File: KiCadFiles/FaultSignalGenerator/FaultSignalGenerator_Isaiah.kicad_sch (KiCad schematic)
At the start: 12 parts, among them U1 OPAMP, U2 TL074CDR

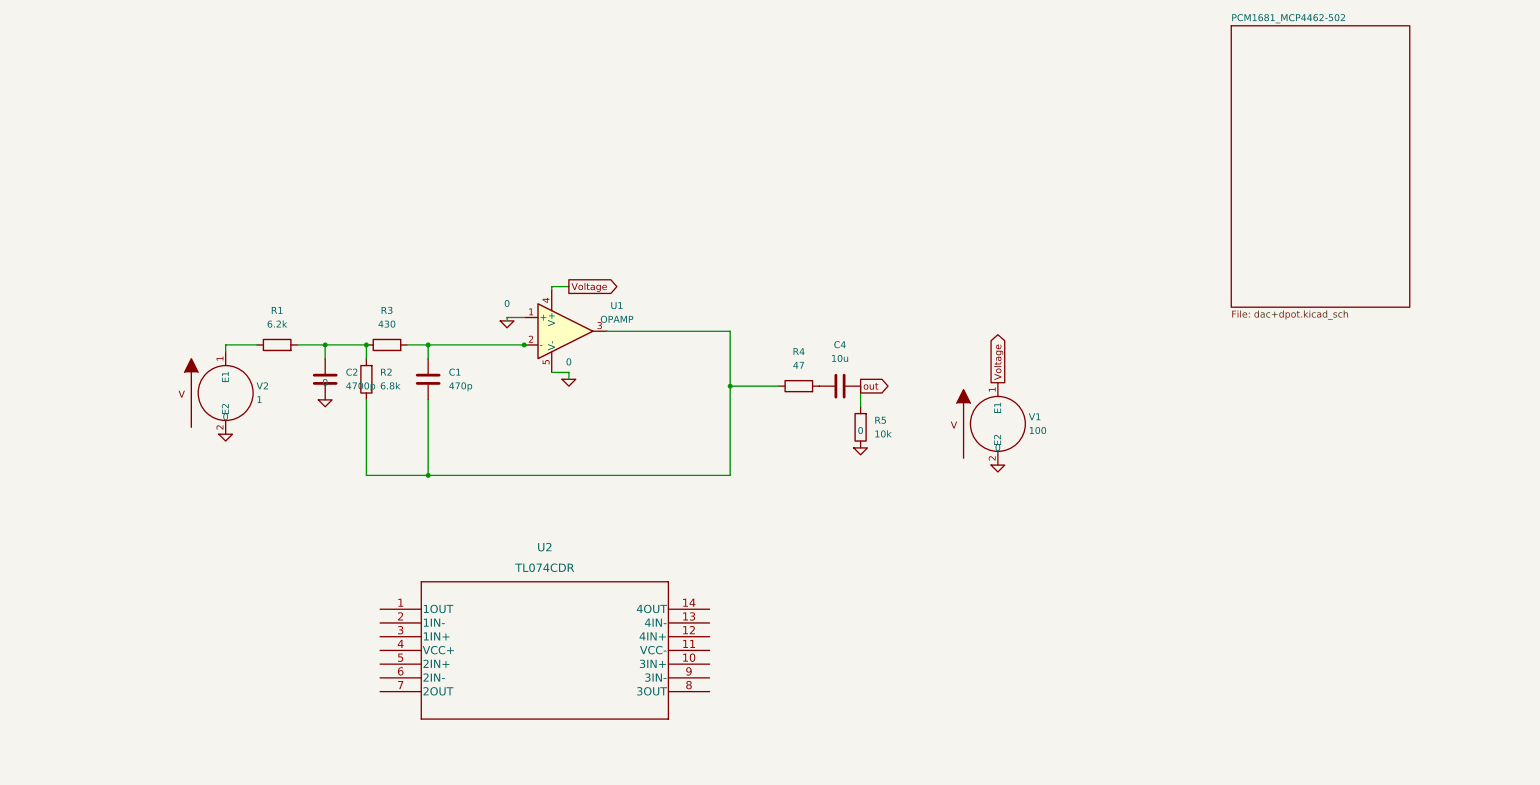
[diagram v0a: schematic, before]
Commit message: Schema push
Got my account stuff sorted out. Push should work now. Still am trying to figure out why my components aren't auto-generating footprints for use in the PCB editor.
Apologies for the messiness.
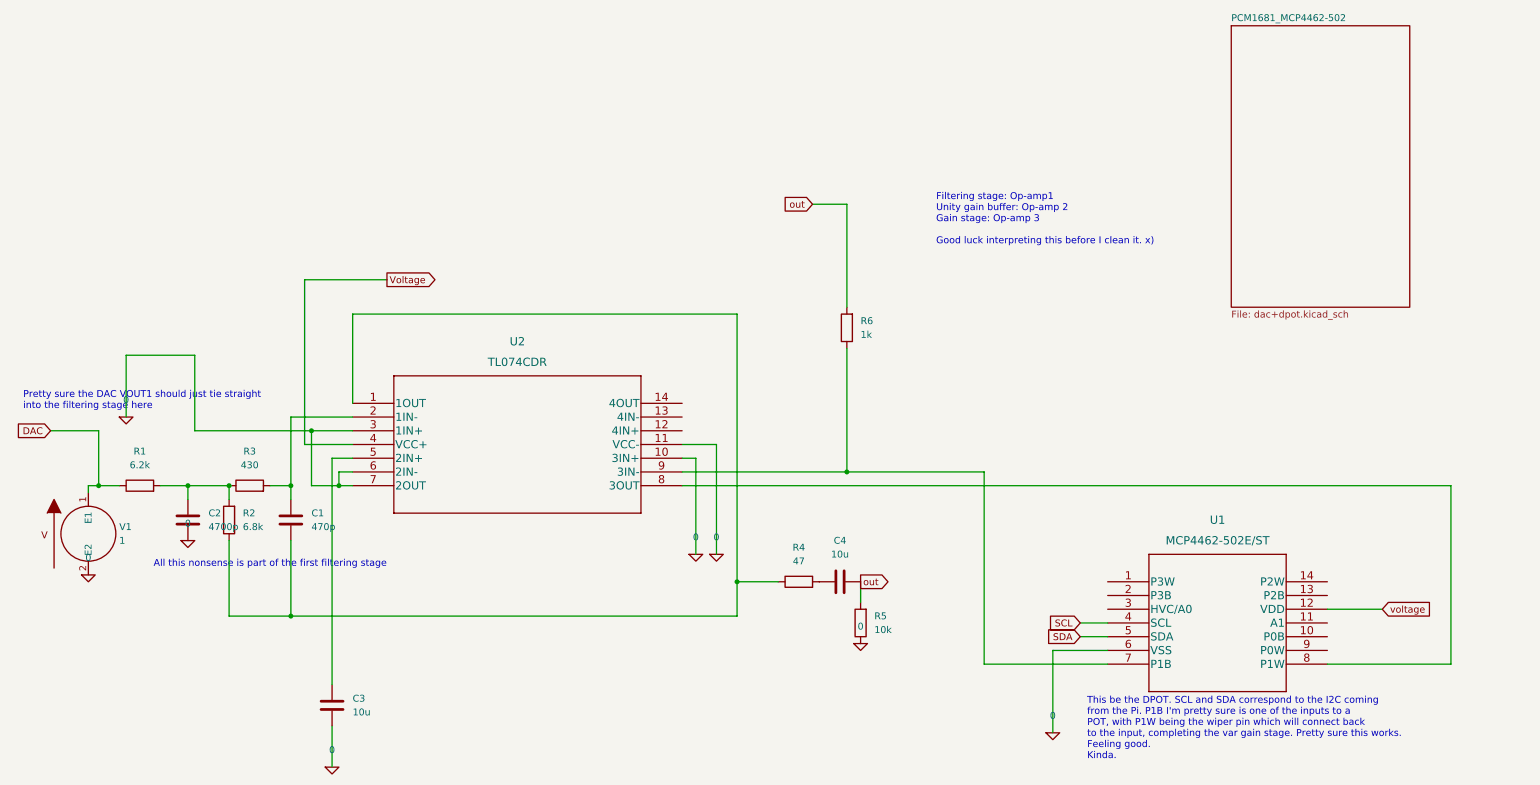
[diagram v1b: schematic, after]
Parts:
- removed U1: OPAMP, symbol Simulation_SPICE:OPAMP
- removed V2: 1, symbol pspice:VSOURCE
- added C3: 10u, symbol Device:C
- added R6: 1k, symbol Device:R
- added U1: MCP4462-502E/ST, TSSOP14_MC_MCH, symbol 2023-01-31_02-59-41:MCP4462-502E/ST
- V1: value 100 -> 1; Spice_Model dc 12 -> dc 50 ac 3
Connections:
- net 0: now also U2.10 (3IN+), U2.11 (VCC-), U2.3 (1IN+), U2.6 (2IN-), U2.7 (2OUT), C3.1, U1.6 (VSS)
- net Voltage: now also U2.4 (VCC+); no longer V1.1 (E1)
- net out: now also R6.2
- net DAC: now reaches R1.1
- net DAC: now also V1.1 (E1)
- net at C1.1, R3.2: now also U2.2 (1IN-)
- net at C1.2, R2.1, R4.1: now also U2.1 (1OUT)
- net at U2.5 (2IN+): now also C3.2
- net at U2.8 (3OUT): now also U1.8 (P1W)
- net at U2.9 (3IN-): now also R6.1, U1.7 (P1B)
- new net SCL: U1.4 (SCL)
- new net SDA: U1.5 (SDA)
- new net voltage: U1.12 (VDD)
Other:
- note added: "All this nonsense is part of the first filtering stage"
- note added: "Filtering stage: Op-amp1 Unity gain buffer: Op-amp 2 Gain stage: Op-amp 3 Good luck interpreting this before I clean it. x)"
- note added: "Pretty sure the DAC VOUT1 should just tie straight into the filtering stage here"
- note added: "This be the DPOT. SCL and SDA correspond to the I2C coming from the Pi. P1B I'm pretty sure is one of the inputs to a POT, with P1W being the wiper pin which will connect back to the input, completing the var gain stage. Pretty sure this works. Feeling good. Kinda."
- moved on the sheet: U2

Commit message: test push
Fully foot-printed schematic
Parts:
- removed V1: 1, symbol pspice:VSOURCE
- C1: renamed from C2; value 4700p -> 4700pF; footprint (none) -> Capacitor_SMD:C_1812_4532Metric_Pad1.57x3.40mm_HandSolder
- C2: renamed from C1; value 470p -> 470pF; footprint (none) -> Capacitor_SMD:C_1812_4532Metric_Pad1.57x3.40mm_HandSolder
- C3: footprint (none) -> Capacitor_SMD:C_1812_4532Metric_Pad1.57x3.40mm_HandSolder
- C4: value 10u -> 10uF; footprint (none) -> Capacitor_SMD:C_1812_4532Metric_Pad1.57x3.40mm_HandSolder
- R1, R2, R3, R4: footprint (none) -> Resistor_SMD:R_0603_1608Metric_Pad0.98x0.95mm_HandSolder
- R5: renamed from R6; footprint (none) -> Resistor_SMD:R_0603_1608Metric_Pad0.98x0.95mm_HandSolder
- R6: renamed from R5; footprint (none) -> Resistor_SMD:R_0603_1608Metric_Pad0.98x0.95mm_HandSolder
- U1: renamed from U2; footprint D14 -> TL074CDR_OpAmp:TL074CDR
- U2: renamed from U1; footprint TSSOP14_MC_MCH -> DPOT:MCP4462-502E&slash_ST
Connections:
- net voltage is gone; now on net +1V5: U2.12 (VDD)
- net Voltage renamed +1V5
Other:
- note added: "DAC VOUT1 should just tie straight into the filtering stage here"
- note added: "Filtering stage: Op-amp1 COM: Op-amp 2 Gain stage: Op-amp 3"
- note added: "This is the DPOT. SCL and SDA correspond to the I2C coming from the Pi. P1B is one of the inputs to a POT, with P1W being the wiper pin which will connect back to the input, completing the var gain stage."
- note removed: "All this nonsense is part of the first filtering stage"
- note removed: "Filtering stage: Op-amp1 Unity gain buffer: Op-amp 2 Gain stage: Op-amp 3 Good luck interpreting this before I clean it. x)"
- note removed: "Pretty sure the DAC VOUT1 should just tie straight into the filtering stage here"
- note removed: "This be the DPOT. SCL and SDA correspond to the I2C coming from the Pi. P1B I'm pretty sure is one of the inputs to a POT, with P1W being the wiper pin which will connect back to the input, completing the var gain stage. Pretty sure this works. Feeling good. Kinda."
- moved on the sheet: R2
